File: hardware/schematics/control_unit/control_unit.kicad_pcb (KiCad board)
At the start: 2 copper layers, 151.8 x 95.4 mm, 138 parts, among them J1 Screw_Terminal_01x12, J2 Screw_Terminal_01x08, J3 Screw_Terminal_01x08, J4 AudioJack4, J5 Screw_Terminal_01x08, J6 6P6C, J7 Conn_01x03_Pin, J8 Conn_01x03_Pin, K1 Relay_SPDT, K2 Relay_SPDT, K3 Relay_SPDT, K4 Relay_SPDT, Q1 2N7000, Q10 IRFZ44N, Q11 IRFZ44N, Q12 IRFZ44N, Q13 IRFZ44N, Q14 IRFZ44N, Q15 IRFZ44N, Q16 IRFZ44N, Q17 IRFZ44N, Q18 2N7000, Q2 2N7000, Q3 IRFZ44N, Q4 IRFZ44N, Q5 IRFZ44N, Q6 2N7000, Q7 2N7000, Q8 IRFZ44N, Q9 IRFZ44N, T1 Transformer_1P_1S, U1 PC817, U10 PC817, U11 PC817, U12 PC817, U13 PC817, U14 MAX487E, U15 ESP-WROOM-32, U16 LM2596T-ADJ, U17 LM35-D, U18 LM324, U2 PC817, U3 PC817, U4 PC817, U5 PC817, U6 PC817, U7 PC817, U8 PC817, U9 PC817

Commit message: fix
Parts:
- J4: footprint HomeMonitor:SCT013 -> PowerMonitor:SCT013
- R44: value 10k -> 1k
- R45: value 18k -> 1.5k
- T1: footprint HomeMonitor:Transformer -> PowerMonitor:Transformer
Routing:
- net Net-(J5-Pin_3): track 21.6 -> 29.2 mm
- net GND: track 1.13 -> 2.65 mm
- net /AC_I_IN_2: track 24.0 -> 23.0 mm
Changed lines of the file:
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@@
 			)
 		)
-		(property "Value" "18k"
+		(property "Value" "1.5k"
 			(at 3.81 2.37 0)
 			(layer "F.Fab")
@@
 			(net 1 "GND")
 			(pintype "passive")
+			(zone_connect 2)
 		)
 		(pad "2" thru_hole circle
@@
 			(net 1 "GND")
 			(pintype "passive")
+			(zone_connect 2)
 		)
 		(model "${KICAD8_3DMODEL_DIR}/Fuse.3dshapes/Fuseholder_Clip-6.3x32mm_Littelfuse_102_Inline_P34.21x7.62mm_D2.54mm_Horizontal.wrl"
@@
 			)
 		)
-		(property "Value" "10k"
+		(property "Value" "1k"
 			(at 3.81 2.37 0)
 			(layer "F.Fab")
@@
 		)
 	)
-	(footprint "HomeMonitor:SCT013"
+	(footprint "PowerMonitor:SCT013"
 		(layer "F.Cu")
 		(at 84.328 108.966)
@@
 		(tags "3.5mm jack mic microphone phones headphones 4pins audio plug")
 		(property "Reference" "J4"
-			(at 0.05 -5.35 0)
+			(at 0 -4.064 0)
 			(layer "F.SilkS")
-			(hide yes)
 			(effects
 				(font
@@
 			(at -0.025 6.35 0)
 			(layer "F.Fab")
-			(hide yes)
 			(effects
 				(font
@@
 			)
 		)
-		(property "Footprint" "HomeMonitor:SCT013"
+		(property "Footprint" "PowerMonitor:SCT013"
 			(at 0 0 0)
 			(unlocked yes)
@@
 		(sheetname "Principale")
 		(sheetfile "control_unit.kicad_sch")
-		(attr smd)
+		(attr through_hole)
 		(fp_line
 			(start -8.375 -2.5)
@@
 		(fp_line
 			(start -6.375 -3.1)
-			(end -4.4 -3.1)
+			(end 5.725 -3.1)
 			(stroke
 				(width 0.12)
@@
 		)
 		(fp_line
-			(start -2 -3.1)
-			(end -1.4 -3.1)
+			(start 5.725 1.7)
+			(end 5.725 -3.1)
 			(stroke
 				(width 0.12)
@@
 		)
 		(fp_line
-			(start 1 -3.1)
-			(end 2.6 -3.1)
+			(start 5.725 2.8)
+			(end 5.725 3.1)
 			(stroke
 				(width 0.12)
@@
 		)
 		(fp_line
-			(start 3.8 3.1)
+			(start 5.725 3.1)
 			(end -6.375 3.1)
 			(stroke
@@
 		)
 		(fp_line
-			(start 5 -3.1)
-			(end 5.725 -3.1)
-			(stroke
-				(width 0.12)
-				(type solid)
-			)
-			(layer "F.SilkS")
-		)
-		(fp_line
-			(start 5.725 2.6)
-			(end 5.725 -3.1)
-			(stroke
-				(width 0.12)
-				(type solid)
-			)
-			(layer "F.SilkS")
-		)
-		(fp_line
 			(start -8.73 -5)
 			(end 6.07 -5)
@@
 		)
 		(pad "R1" thru_hole oval
-			(at -0.175 -3.25)
+			(at -0.2 -2.25)
 			(size 2 1)
 			(drill oval 1 0.5)
@@
 		)
 		(pad "R2" thru_hole oval
-			(at -3.175 -3.25)
+			(at -3.2 -2.25)
 			(size 2 1)
 			(drill oval 1 0.5)
@@
 		)
 		(pad "S" thru_hole oval
-			(at 4.925 3.25)
+			(at 4.9 2.25)
 			(size 2 1)
 			(drill oval 1 0.5)
@@
 		)
 		(pad "T" thru_hole oval
-			(at 3.825 -3.25)
+			(at 3.8 -2.25)
 			(size 2 1)
 			(drill oval 1 0.5)
@@
 			)
 		)
-		(pad "1" thru_hole circle
+		(pad "1" thru_hole oval
 			(at 7.25 2.5)
-			(size 1.6 1.6)
-			(drill 0.8)
+			(size 2.3 1.8)
+			(drill 1.5)
 			(layers "*.Cu" "*.Mask")
 			(remove_unused_layers no)
@@
 		)
 	)
-	(footprint "HomeMonitor:Transformer"
+	(footprint "PowerMonitor:Transformer"
 		(layer "F.Cu")
 		(at 118.004 117.512)
 		(property "Reference" "T1"
-			(at 9.25 -0.926 0)
+			(at 8.996 -0.926 0)
 			(unlocked yes)
 			(layer "F.SilkS")
@@
 			)
 		)
-		(property "Footprint" "HomeMonitor:Transformer"
+		(property "Footprint" "PowerMonitor:Transformer"
 			(at 15.25 -5.5 0)
 			(unlocked yes)
@@
 	)
 	(segment
+		(start 198.354 144.272)
+		(end 198.354 142.7534)
+		(width 0.508)
+		(layer "B.Cu")
+		(net 1)
+	)
+	(segment
 		(start 121.198 128.484)
 		(end 121.158 128.524)
@@
 	)
 	(segment
-		(start 79.756 116.332)
-		(end 79.756 108.458)
+		(start 128.504 124.166997)
+		(end 128.524 124.186997)
 		(width 0.254)
 		(layer "F.Cu")
@@
 	)
 	(segment
-		(start 128.504 124.166997)
-		(end 128.524 124.186997)
+		(start 108.712 122.428)
+		(end 109.22 122.936)
 		(width 0.254)
 		(layer "F.Cu")
@@
 	)
 	(segment
-		(start 108.712 122.428)
-		(end 109.22 122.936)
+		(start 79.756 109.982)
+		(end 81.128 108.61)
 		(width 0.254)
 		(layer "F.Cu")
@@
 	)
 	(segment
+		(start 89.154 116.332)
+		(end 83.566 116.332)
+		(width 0.254)
+		(layer "F.Cu")
+		(net 5)
+	)
+	(segment
 		(start 109.22 122.936)
 		(end 109.22 128.524)
@@
 	)
 	(segment
-		(start 79.756 108.458)
-		(end 81.153 107.061)
+		(start 89.228 116.258)
+		(end 89.154 116.332)
 		(width 0.254)
 		(layer "F.Cu")
@@
 	)
 	(segment
-		(start 89.253 116.431)
-		(end 89.253 112.216)
+		(start 89.228 111.216)
+		(end 89.228 116.258)
+		(width 0.254)
+		(layer "F.Cu")
+		(net 5)
+	)
+	(segment
+		(start 81.128 108.61)
+		(end 81.128 106.716)
 		(width 0.254)
 		(layer "F.Cu")
@@
 	)
 	(segment
-		(start 81.153 107.061)
-		(end 81.153 105.716)
+		(start 128.524 132.261)
+		(end 128.524 129.105)
 		(width 0.254)
 		(layer "F.Cu")
@@
 	)
 	(segment
-		(start 128.524 132.261)
-		(end 128.524 129.105)
+		(start 91.948 119.126)
+		(end 91.948 121.412)
+		(width 0.254)
+		(layer "F.Cu")
+		(net 5)
+	)
+	(segment
+		(start 79.756 116.332)
+		(end 79.756 109.982)
 		(width 0.254)
 		(layer "F.Cu")
@@
 	(segment
 		(start 91.948 119.126)
-		(end 91.948 121.412)
+		(end 89.154 116.332)
 		(width 0.254)
 		(layer "F.Cu")
@@
 	)
 	(segment
-		(start 89.154 116.332)
-		(end 91.948 119.126)
-		(width 0.254)
-		(layer "F.Cu")
-		(net 5)
-	)
-	(segment
-		(start 83.566 116.332)
-		(end 89.154 116.332)
-		(width 0.254)
-		(layer "F.Cu")
-		(net 5)
-	)
-	(segment
 		(start 109.22 143.256)
 		(end 109.728 143.764)
@@
 	)
 	(segment
-		(start 90.678 106.172)
-		(end 90.222 105.716)
+		(start 91.186 116.332)
+		(end 91.186 111.252)
 		(width 0.254)
 		(layer "F.Cu")
@@
 	)
 	(segment
-		(start 90.678 110.744)
-		(end 90.678 106.172)
+		(start 91.186 111.252)
+		(end 90.678 110.744)
 		(width 0.254)
 		(layer "F.Cu")
@@
 	)
 	(segment
-		(start 90.222 105.716)
-		(end 88.153 105.716)
+		(start 90.678 107.188)
+		(end 90.206 106.716)
 		(width 0.254)
 		(layer "F.Cu")
@@
 	)
 	(segment
-		(start 91.186 116.332)
-		(end 91.186 111.252)
+		(start 90.678 110.744)
+		(end 90.678 107.188)
 		(width 0.254)
 		(layer "F.Cu")
@@
 	)
 	(segment
-		(start 91.186 111.252)
-		(end 90.678 110.744)
+		(start 90.206 106.716)
+		(end 88.128 106.716)
 		(width 0.254)
 		(layer "F.Cu")
@@
 	)
 	(segment
+		(start 104.394 72.254)
+		(end 104.394 64.634)
+		(width 2.032)
+		(layer "B.Cu")
+		(net 122)
+	)
+	(segment
 		(start 111.998 98.023)
 		(end 112.263 98.288)
@@
 		(layer "B.Cu")
 		(hatch edge 0.5)
-		(connect_pads yes
+		(connect_pads
 			(clearance 0.5)
 		)

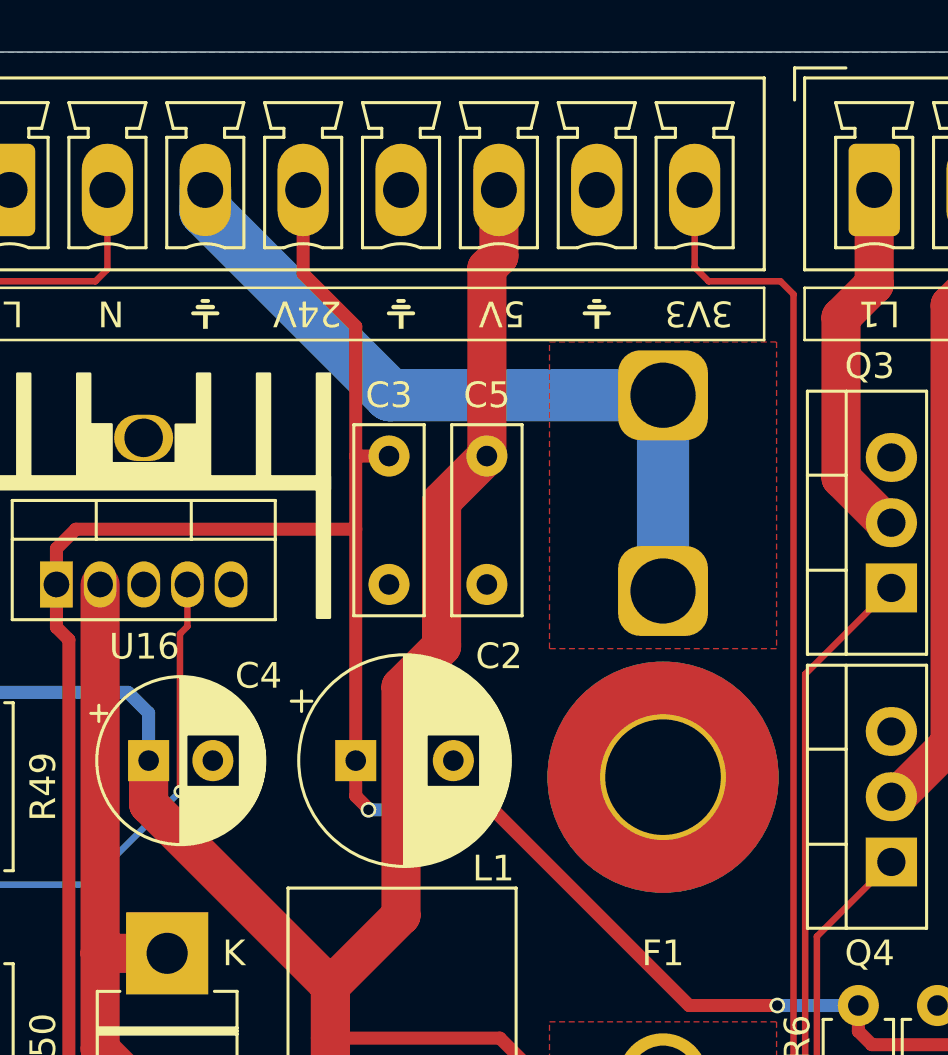
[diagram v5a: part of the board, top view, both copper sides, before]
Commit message: feat: screw to fuse-
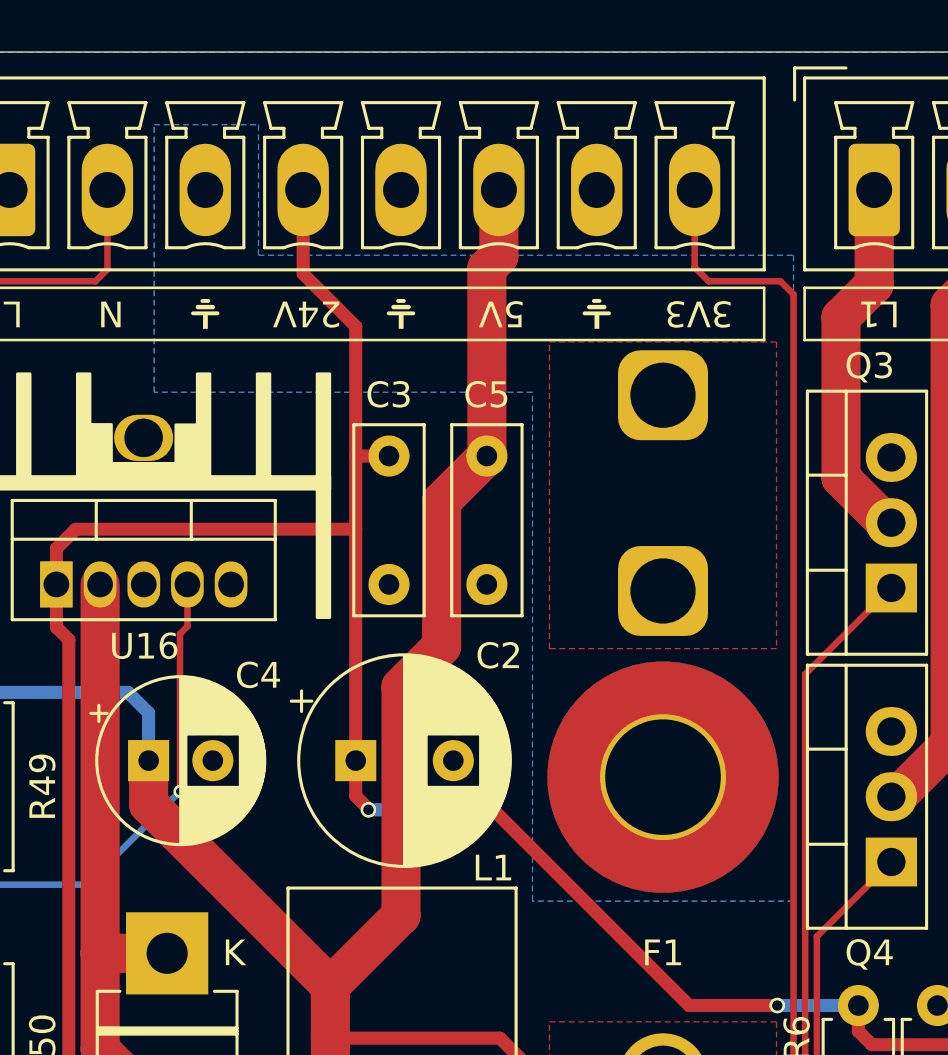
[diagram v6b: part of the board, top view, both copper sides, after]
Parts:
- H1: value MountingHole -> MountingHole_Pad
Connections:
- F1 pad 1: Net-(J5-Pin_3) -> /F-
- H1 pad 1: (no net) -> /F-
- J5 pad 3: Net-(J5-Pin_3) -> /F-
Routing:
- net Net-(J5-Pin_3): track 29.2 -> 0.00 mm
- added copper zone on B.Cu, net /F-
- added copper zone on F.Cu, net /F-
- removed copper zone on F.Cu, net Net-(J5-Pin_3)

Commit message: chore
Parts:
- removed the G*** at (86.6, 61.5)
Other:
- board text added: "-"
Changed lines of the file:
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@@
 		)
 	)
-	(footprint "LOGO"
-		(layer "F.Cu")
-		(at 86.57493 61.468 180)
-		(property "Reference" "G***"
-			(at 0 0 0)
-			(layer "F.SilkS")
-			(hide yes)
-			(effects
-				(font
-					(size 1.5 1.5)
-					(thickness 0.3)
-				)
-			)
-		)
-		(property "Value" "LOGO"
-			(at 0.75 0 0)
-			(layer "F.SilkS")
-			(hide yes)
-			(effects
-				(font
-					(size 1.5 1.5)
-					(thickness 0.3)
-				)
-			)
-		)
-		(property "Footprint" ""
-			(at 0 0 0)
-			(layer "F.Fab")
-			(hide yes)
-			(effects
-				(font
-					(size 1.27 1.27)
-					(thickness 0.15)
-				)
-			)
-		)
-		(property "Datasheet" ""
-			(at 0 0 0)
-			(layer "F.Fab")
-			(hide yes)
-			(effects
-				(font
-					(size 1.27 1.27)
-					(thickness 0.15)
-				)
-			)
-		)
-		(property "Description" ""
-			(at 0 0 0)
-			(layer "F.Fab")
-			(hide yes)
-			(effects
-				(font
-					(size 1.27 1.27)
-					(thickness 0.15)
-				)
-			)
-		)
-		(attr board_only exclude_from_pos_files exclude_from_bom)
-		(fp_poly
-			(pts
-				(xy 0.317626 0.183524) (xy 0.33099 0.189462) (xy 0.343127 0.197322) (xy 0.353805 0.206852) (xy 0.362791 0.217796)
-				(xy 0.369852 0.229901) (xy 0.374758 0.242915) (xy 0.375779 0.246979) (xy 0.377277 0.257291) (xy 0.377547 0.268479)
-				(xy 0.376638 0.279637) (xy 0.374601 0.289855) (xy 0.373198 0.294262) (xy 0.366812 0.308087) (xy 0.358502 0.320314)
-				(xy 0.348372 0.330846) (xy 0.336529 0.339584) (xy 0.32308 0.346431) (xy 0.312124 0.350233) (xy 0.302471 0.352988)
-				(xy 0.00442 0.353155) (xy -0.022953 0.353165) (xy -0.04972 0.353167) (xy -0.075765 0.353159) (xy -0.100975 0.353143)
-				(xy -0.125235 0.353118) (xy -0.148431 0.353085) (xy -0.170448 0.353045) (xy -0.191173 0.352998)
-				(xy -0.210491 0.352943) (xy -0.228287 0.352882) (xy -0.244449 0.352815) (xy -0.258861 0.352742)
-				(xy -0.271408 0.352664) (xy -0.281978 0.35258) (xy -0.290455 0.352491) (xy -0.296725 0.352398) (xy -0.300675 0.352301)
-				(xy -0.302081 0.352221) (xy -0.315985 0.34917) (xy -0.32922 0.343842) (xy -0.341474 0.336466) (xy -0.352432 0.327265)
-				(xy -0.36178 0.316466) (xy -0.369204 0.304294) (xy -0.369456 0.303782) (xy -0.374902 0.28993) (xy -0.377903 0.275863)
-				(xy -0.378499 0.261809) (xy -0.376726 0.247992) (xy -0.372623 0.234638) (xy -0.366228 0.221972)
-				(xy -0.357579 0.210221) (xy -0.352904 0.205234) (xy -0.342475 0.196215) (xy -0.331214 0.189186)
-				(xy -0.318418 0.183713) (xy -0.317686 0.183459) (xy -0.307523 0.179967) (xy 0 0.179967) (xy 0.307523 0.179967)
-			)
-			(stroke
-				(width 0)
-				(type solid)
-			)
-			(fill solid)
-			(layer "F.SilkS")
-		)
-		(fp_poly
-			(pts
-				(xy 0.002526 0.428764) (xy 0.022477 0.428767) (xy 0.040064 0.428777) (xy 0.055448 0.428798) (xy 0.068793 0.428831)
-				(xy 0.080259 0.428881) (xy 0.090008 0.42895) (xy 0.098202 0.42904) (xy 0.105004 0.429155) (xy 0.110575 0.429298)
-				(xy 0.115076 0.429472) (xy 0.11867 0.429678) (xy 0.121519 0.429921) (xy 0.123784 0.430203) (xy 0.125627 0.430527)
-				(xy 0.12721 0.430895) (xy 0.127556 0.430987) (xy 0.140933 0.43579) (xy 0.15296 0.442479) (xy 0.163466 0.450843)
-				(xy 0.17228 0.460672) (xy 0.17923 0.471754) (xy 0.184145 0.483879) (xy 0.186854 0.496836) (xy 0.187345 0.50454)
-				(xy 0.186947 0.515009) (xy 0.185318 0.524276) (xy 0.182215 0.533467) (xy 0.179913 0.538639) (xy 0.173015 0.550252)
-				(xy 0.164062 0.560479) (xy 0.153203 0.56917) (xy 0.145237 0.5739) (xy 0.142686 0.57525) (xy 0.140378 0.576446)
-				(xy 0.138153 0.577496) (xy 0.135848 0.57841) (xy 0.133301 0.579198) (xy 0.130353 0.579868) (xy 0.126839 0.580431)
-				(xy 0.1226 0.580894) (xy 0.117473 0.581268) (xy 0.111298 0.581561) (xy 0.103911 0.581784) (xy 0.095152 0.581944)
-				(xy 0.08486 0.582052) (xy 0.072872 0.582117) (xy 0.059026 0.582148) (xy 0.043163 0.582154) (xy 0.025118 0.582145)
-				(xy 0.004732 0.582129) (xy 0.001712 0.582127) (xy -0.018909 0.582107) (xy -0.037154 0.582078) (xy -0.053173 0.582037)
-				(xy -0.067113 0.581982) (xy -0.079126 0.581909) (xy -0.08936 0.581818) (xy -0.097966 0.581706) (xy -0.105091 0.581571)
-				(xy -0.110887 0.58141) (xy -0.115502 0.581221) (xy -0.119085 0.581002) (xy -0.121787 0.58075) (xy -0.123757 0.580464)
-				(xy -0.124889 0.580214) (xy -0.138046 0.575417) (xy -0.149885 0.56855) (xy -0.160224 0.559795) (xy -0.168885 0.549335)
-				(xy -0.175689 0.537355) (xy -0.180454 0.524036) (xy -0.180635 0.523342) (xy -0.182726 0.510282)
-				(xy -0.182419 0.497326) (xy -0.179836 0.484729) (xy -0.175101 0.472747) (xy -0.168336 0.461635)
-				(xy -0.159664 0.451649) (xy -0.149208 0.443047) (xy -0.139238 0.437127) (xy -0.136536 0.435757)
-				(xy -0.134085 0.434545) (xy -0.131721 0.433481) (xy -0.129278 0.432557) (xy -0.126592 0.431762)
-				(xy -0.123498 0.431086) (xy -0.119833 0.43052) (xy -0.115431 0.430054) (xy -0.110128 0.429679) (xy -0.103759 0.429384)
-				(xy -0.096159 0.42916) (xy -0.087165 0.428997) (xy -0.076612 0.428886) (xy -0.064334 0.428817) (xy -0.050169 0.42878)
-				(xy -0.03395 0.428765) (xy -0.015513 0.428763)
-			)
-			(stroke
-				(width 0)
-				(type solid)
-			)
-			(fill solid)
-			(layer "F.SilkS")
-		)
-		(fp_poly
-			(pts
-				(xy 0.088405 -0.317003) (xy 0.088405 -0.053043) (xy 0.285851 -0.053043) (xy 0.311987 -0.053042)
-				(xy 0.335719 -0.053039) (xy 0.35717 -0.053032) (xy 0.376463 -0.05302) (xy 0.39372 -0.053001) (xy 0.409064 -0.052974)
-				(xy 0.422617 -0.052938) (xy 0.434501 -0.05289) (xy 0.44484 -0.052829) (xy 0.453756 -0.052755) (xy 0.461371 -0.052664)
-				(xy 0.467807 -0.052557) (xy 0.473188 -0.052431) (xy 0.477635 -0.052285) (xy 0.481272 -0.052118)
-				(xy 0.48422 -0.051928) (xy 0.486603 -0.051713) (xy 0.488543 -0.051472) (xy 0.490161 -0.051204) (xy 0.491582 -0.050907)
-				(xy 0.492926 -0.05058) (xy 0.493052 -0.050548) (xy 0.50326 -0.047291) (xy 0.512234 -0.042901) (xy 0.520695 -0.036955)
-				(xy 0.528669 -0.029725) (xy 0.537126 -0.020252) (xy 0.543365 -0.010622) (xy 0.547551 -0.000395)
-				(xy 0.549852 0.010867) (xy 0.550435 0.023602) (xy 0.550325 0.027231) (xy 0.54963 0.036652) (xy 0.548327 0.044375)
-				(xy 0.546195 0.051199) (xy 0.543013 0.057922) (xy 0.540804 0.061754) (xy 0.532522 0.073044) (xy 0.522352 0.082687)
-				(xy 0.510381 0.090613) (xy 0.499161 0.095828) (xy 0.490647 0.09914) (xy 0.003789 0.099377) (xy -0.038493 0.099396)
-				(xy -0.078322 0.099413) (xy -0.115768 0.099426) (xy -0.150906 0.099435) (xy -0.183806 0.099441)
-				(xy -0.214542 0.099442) (xy -0.243185 0.099439) (xy -0.269807 0.099431) (xy -0.294481 0.099418)
-				(xy -0.317279 0.099401) (xy -0.338273 0.099378) (xy -0.357535 0.099349) (xy -0.375138 0.099315)
-				(xy -0.391153 0.099275) (xy -0.405653 0.099228) (xy -0.418711 0.099175) (xy -0.430397 0.099116)
-				(xy -0.440785 0.099049) (xy -0.449946 0.098975) (xy -0.457953 0.098894) (xy -0.464878 0.098805)
-				(xy -0.470793 0.098709) (xy -0.475771 0.098604) (xy -0.479883 0.098491) (xy -0.483202 0.098369)
-				(xy -0.4858 0.098239) (xy -0.487749 0.098099) (xy -0.489121 0.09795) (xy -0.489989 0.097792) (xy -0.490016 0.097785)
-				(xy -0.503101 0.093131) (xy -0.514895 0.086518) (xy -0.525217 0.078173) (xy -0.533885 0.068322)
-				(xy -0.540716 0.057193) (xy -0.545529 0.045013) (xy -0.548142 0.03201) (xy -0.548575 0.024627) (xy -0.547712 0.011042)
-				(xy -0.544783 -0.001244) (xy -0.539664 -0.01253) (xy -0.532232 -0.023117) (xy -0.526143 -0.029725)
-				(xy -0.517514 -0.037481) (xy -0.509039 -0.043292) (xy -0.499996 -0.047579) (xy -0.490526 -0.050548)
-				(xy -0.489161 -0.050883) (xy -0.487731 -0.051187) (xy -0.486112 -0.051461) (xy -0.484179 -0.051707)
-				(xy -0.481808 -0.051926) (xy -0.478874 -0.052119) (xy -0.475251 -0.052289) (xy -0.470816 -0.052437)
-				(xy -0.465444 -0.052564) (xy -0.45901 -0.052672) (xy -0.451388 -0.052762) (xy -0.442456 -0.052836)
-				(xy -0.432087 -0.052896) (xy -0.420157 -0.052943) (xy -0.406541 -0.052979) (xy -0.391115 -0.053005)
-				(xy -0.373754 -0.053023) (xy -0.354333 -0.053034) (xy -0.332727 -0.05304) (xy -0.308813 -0.053042)
-				(xy -0.289643 -0.053043) (xy -0.098514 -0.053043) (xy -0.098196 -0.316679) (xy -0.097877 -0.580315)
-				(xy -0.004736 -0.580639) (xy 0.088405 -0.580962)
-			)
-			(stroke
-				(width 0)
-				(type solid)
-			)
-			(fill solid)
-			(layer "F.SilkS")
-		)
-	)
 	(footprint "Package_TO_SOT_THT:TO-220-3_Vertical"
 		(layer "F.Cu")
@@
 		(layer "F.SilkS")
 		(effects
+			(font
+				(size 1 1)
+				(thickness 0.15)
+			)
+			(justify left bottom)
+		)
+	)
+	(gr_text "-"
+		(at 87.318048 60.865654 180)
+		(layer "F.SilkS")
+		(effects

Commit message: fix: powermonitor lower resistor to 680ohm
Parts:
- R59: value 820 -> 680
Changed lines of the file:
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@@
 			)
 		)
-		(property "Value" "820"
+		(property "Value" "680"
 			(at 3.81 2.37 0)
 			(layer "F.Fab")
